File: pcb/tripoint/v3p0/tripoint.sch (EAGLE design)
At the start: 19 parts, among them IC1 ATMEGA325P, IC2 LM340MP-05, J1 DCJ0202

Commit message: added board layout for TriPoint
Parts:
- removed C1: 220nF, rcl:C-EUC0805
- removed C2: 100nF, rcl:C-EUC0805
- removed C3, C4, C5, C6, C7: 100nF, rcl:C-EUC0603
- removed IC1: ATMEGA325P, atmel:ATMEGA325P
- removed IC2: LM340MP-05, linear:LM340MP-05
- removed J1: DCJ0202, con-jack:DCJ0202
- removed LED1, LED2: GREEN, led:LEDCHIP-LED0603
- removed QF1: 16M20AUM1, crystal:16M20AUM1
- removed R1: 10k, rcl:R-US_R0603
- removed R2, R3: 150, rcl:R-US_R0603
- removed S1: (no value), switch-omron:10-XX
- removed SV1: (no value), con-lstb:MA03-2
- removed SV2: (no value), con-lstb:MA08-1
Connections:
- removed net +3V3: C2.1, C4.1, C5.1, IC1.OC1B/PCINT14/PB6, IC1.XCK/AIN0/PCINT2/PE2, IC2.VO, R1.2, R2.2, SV1.5
- removed net GND: C1.2, C2.2, C3.2, C4.2, C5.2, C6.2, C7.2, IC1.DO/PCINT6/PE6, IC1.OC1A/PCINT13/PB5, IC2.GND, J1.2, J1.3, LED1.C, LED2.C, S1.P, S1.P1, SV1.1
- removed net MISO: IC1.PD7, SV1.6
- removed net MOSI: IC1.PD5, SV1.3
- removed net N$1: C1.1, IC2.VI, J1.1
- removed net N$12: IC1.AREF, SV2.3
- removed net N$13: IC1.ADC0/PF0, SV2.4
- removed net N$14: IC1.ADC1/PF1, SV2.5
- removed net N$15: IC1.ADC2/PF2, SV2.6
- removed net N$16: IC1.ADC3/PF3, SV2.7
- removed net N$17: IC1.ADC4/TCK/PF4, SV2.8
- removed net N$2: C3.1, IC1.AIN1/PCINT3/PE3
- removed net N$3: C6.1, IC1.PA3, QF1.3
- removed net N$4: C7.1, IC1.PA4, QF1.1
- removed net N$5: IC1.AVCC, SV2.1
- removed net N$6: LED1.A, R2.1
- removed net N$7: IC1.GND@2, SV2.2
- removed net N$8: LED2.A, R3.1
- removed net RESET: IC1.OC2A/PCINT15/PB7, R1.1, S1.S, S1.S1, SV1.2
- removed net SCK: IC1.PD6, R3.2, SV1.4

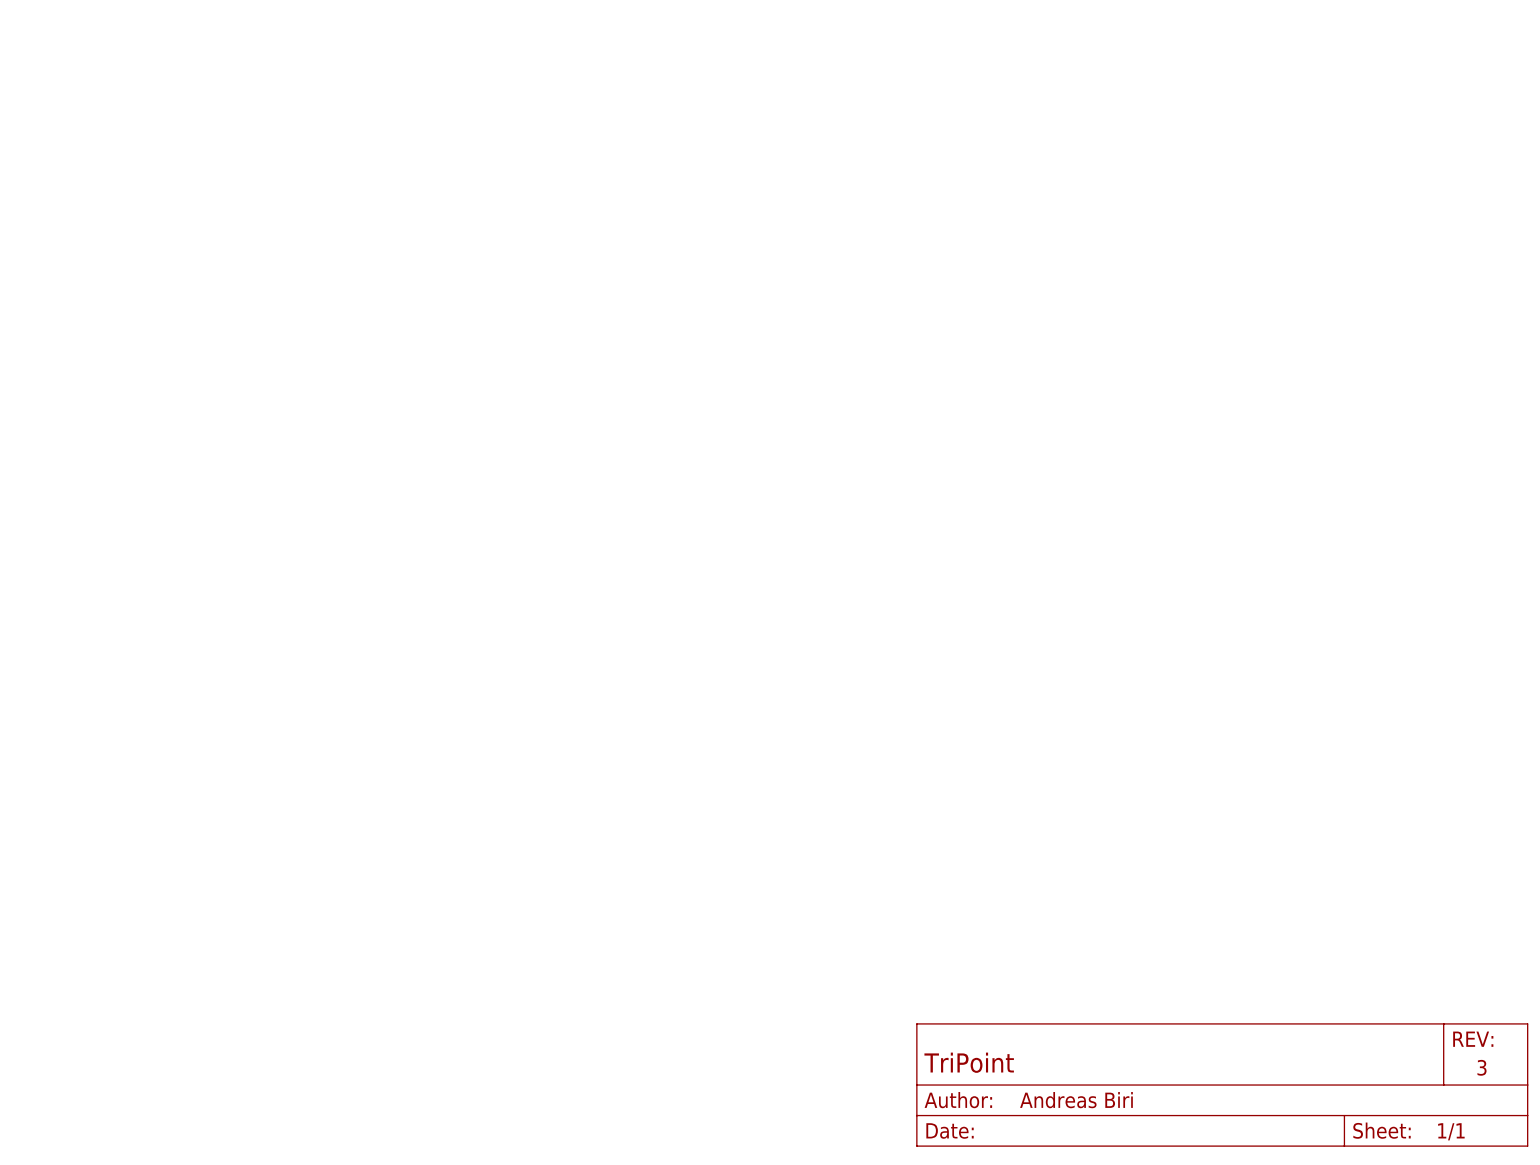
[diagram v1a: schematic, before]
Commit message: populated schematic without STM connections
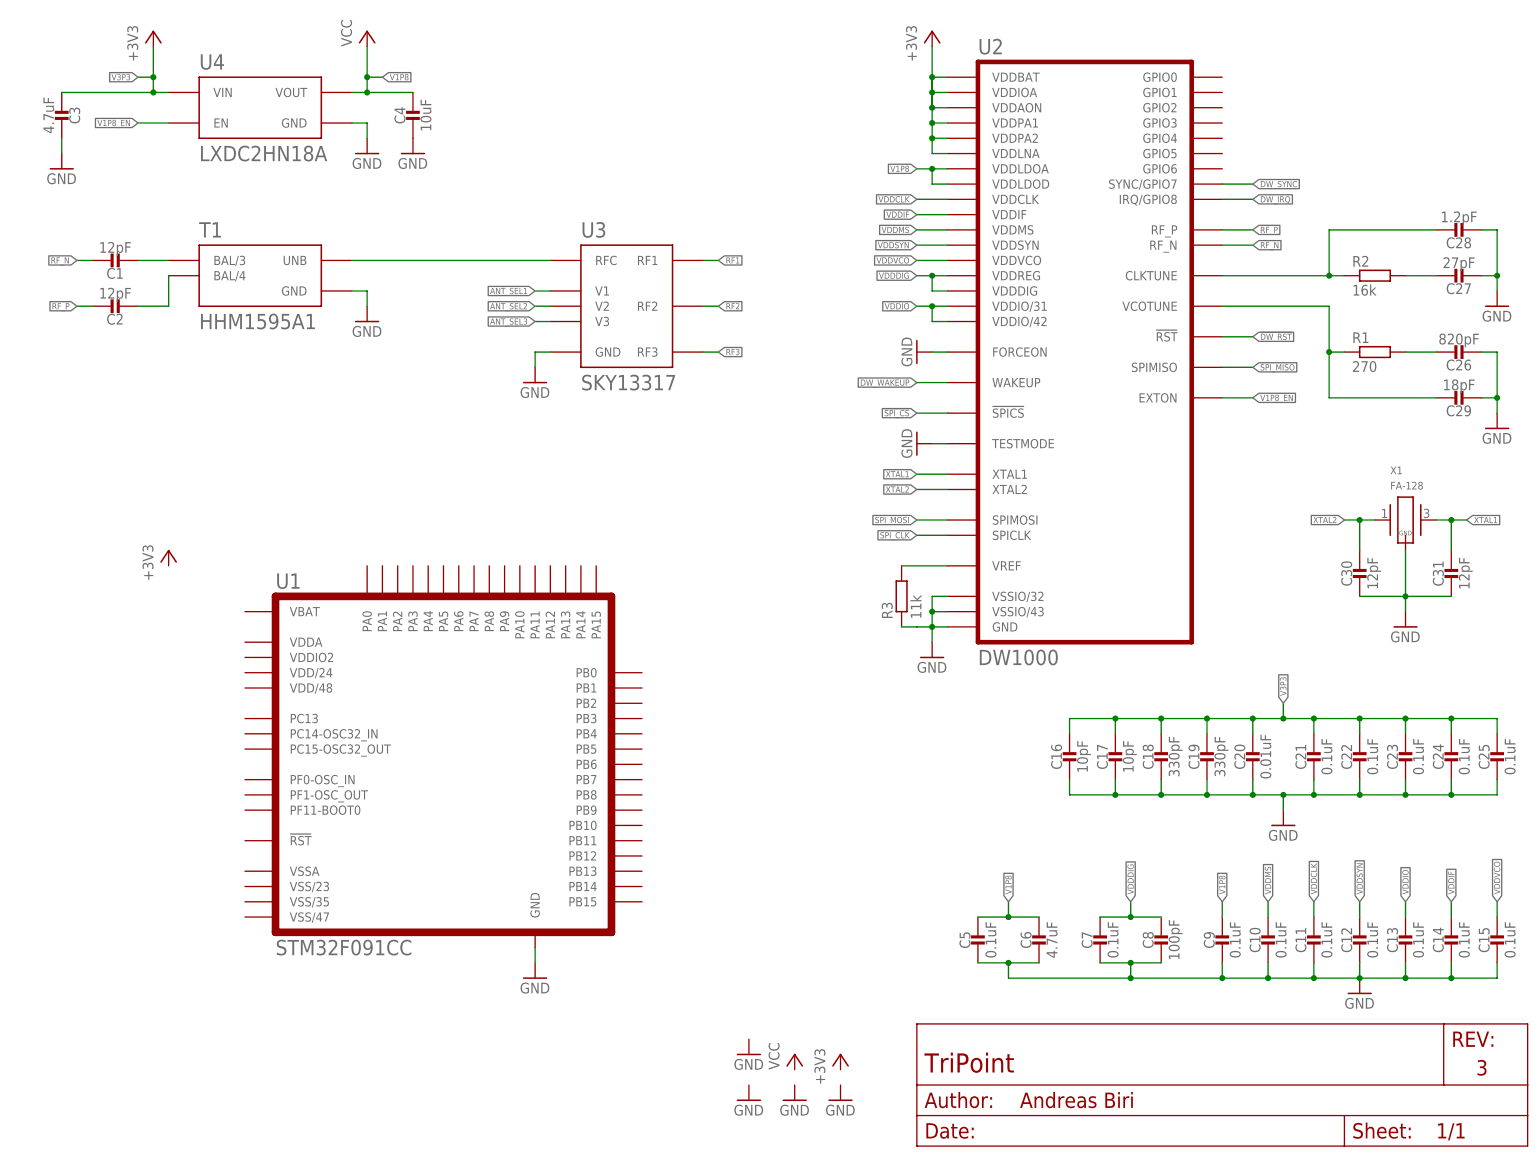
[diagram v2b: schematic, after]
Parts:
- added C1, C2, C30, C31: 12pF, passives:CAPACITOR0201_CAP
- added C10, C11, C12, C13, C14, C15, C21, C22, C23, C24, C25, C5, C7, C9: 0.1uF, passives:CAPACITOR0201_CAP
- added C16, C17: 10pF, passives:CAPACITOR0201_CAP
- added C18, C19: 330pF, passives:CAPACITOR0201_CAP
- added C20: 0.01uF, passives:CAPACITOR0201_CAP
- added C26: 820pF, passives:CAPACITOR0201_CAP
- added C27: 27pF, passives:CAPACITOR0201_CAP
- added C28: 1.2pF, passives:CAPACITOR0201_CAP
- added C29: 18pF, passives:CAPACITOR0201_CAP
- added C3, C6: 4.7uF, passives:CAPACITOR0603_CAP
- added C4: 10uF, passives:CAPACITOR0603_CAP
- added C8: 100pF, passives:CAPACITOR0201_CAP
- added R1: 270, rcl:R-EU_R0201
- added R2: 16k, rcl:R-EU_R0201
- added R3: 11k, rcl:R-EU_R0201
- added T1: HHM1595A1, rf:HHM1595A1
- added U1: STM32F091CC, chips:STM32F091CC
- added U2: DW1000, chips:DW1000
- added U3: SKY13317, switches:SKY13317
- added U4: LXDC2HN18A, regulators:LXDC2HN18A
- added X1: FA-128, crystals:FA-128
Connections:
- new net !DW_RST: U2.!RST
- new net !SPI_CS: U2.!SPICS
- new net ANT_SEL1: U3.V1
- new net ANT_SEL2: U3.V2
- new net ANT_SEL3: U3.V3
- new net DW_IRQ: U2.IRQ/GPIO8
- new net DW_SYNC: U2.SYNC/GPIO7
- new net DW_WAKEUP: U2.WAKEUP
- new net GND: C10.2, C11.2, C12.2, C13.2, C14.2, C15.2, C16.2, C17.2, C18.2, C19.2, C20.2, C21.2, C22.2, C23.2, C24.2, C25.2, C26.2, C27.2, C28.2, C29.2, C3.1, C30.2, C31.2, C4.2, C5.2, C6.2, C7.2, C8.2, C9.2, R3.1, T1.GND, U1.GND, U2.FORCEON, U2.GND, U2.TESTMODE, U2.VSSIO/32, U2.VSSIO/43, U3.GND, U4.GND, X1.GND
- new net N$1: T1.UNB, U3.RFC
- new net N$2: C1.2, T1.BAL/3
- new net N$3: C2.2, T1.BAL/4
- new net N$4: C26.1, R1.2
- new net N$5: C27.1, R2.2
- new net N$6: C29.1, R1.1, U2.VCOTUNE
- new net N$7: R3.2, U2.VREF
- new net N$9: C28.1, R2.1, U2.CLKTUNE
- new net RF1: U3.RF1
- new net RF2: U3.RF2
- new net RF3: U3.RF3
- new net RF_N: C1.1, U2.RF_N
- new net RF_P: C2.1, U2.RF_P
- new net SPI_CLK: U2.SPICLK
- new net SPI_MISO: U2.SPIMISO
- new net SPI_MOSI: U2.SPIMOSI
- new net V1P8: C4.1, C5.1, C6.1, C9.1, U2.VDDLDOA, U2.VDDLDOD, U4.VOUT
- new net V1P8_EN: U2.EXTON, U4.EN
- new net V3P3: C16.1, C17.1, C18.1, C19.1, C20.1, C21.1, C22.1, C23.1, C24.1, C25.1, C3.2, U2.VDDAON, U2.VDDBAT, U2.VDDIOA, U2.VDDLNA, U2.VDDPA1, U2.VDDPA2, U4.VIN
- new net VDDCLK: C11.1, U2.VDDCLK
- new net VDDDIG: C7.1, C8.1, U2.VDDDIG, U2.VDDREG
- new net VDDIF: C14.1, U2.VDDIF
- new net VDDIO: C13.1, U2.VDDIO/31, U2.VDDIO/42
- new net VDDMS: C10.1, U2.VDDMS
- new net VDDSYN: C12.1, U2.VDDSYN
- new net VDDVCO: C15.1, U2.VDDVCO
- new net XTAL1: C31.1, U2.XTAL1, X1.2
- new net XTAL2: C30.1, U2.XTAL2, X1.1
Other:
- note added: "VDDLDOA"
- note added: "VDDLDOD"
